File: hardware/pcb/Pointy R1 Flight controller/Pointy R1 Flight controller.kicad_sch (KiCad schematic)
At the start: 28 parts, among them IC1 TEENSY_4.1, J3 XT60-M, M1 Motor_Servo, M2 Motor_Servo, P1 282837-2, P2 282837-2, P3 282837-2, P5 282837-2, Q1 2N7002, Q2 2N7002, Q3 2N7002, U1 L7805CV, U2 GY-521, U3 MPL3115A2

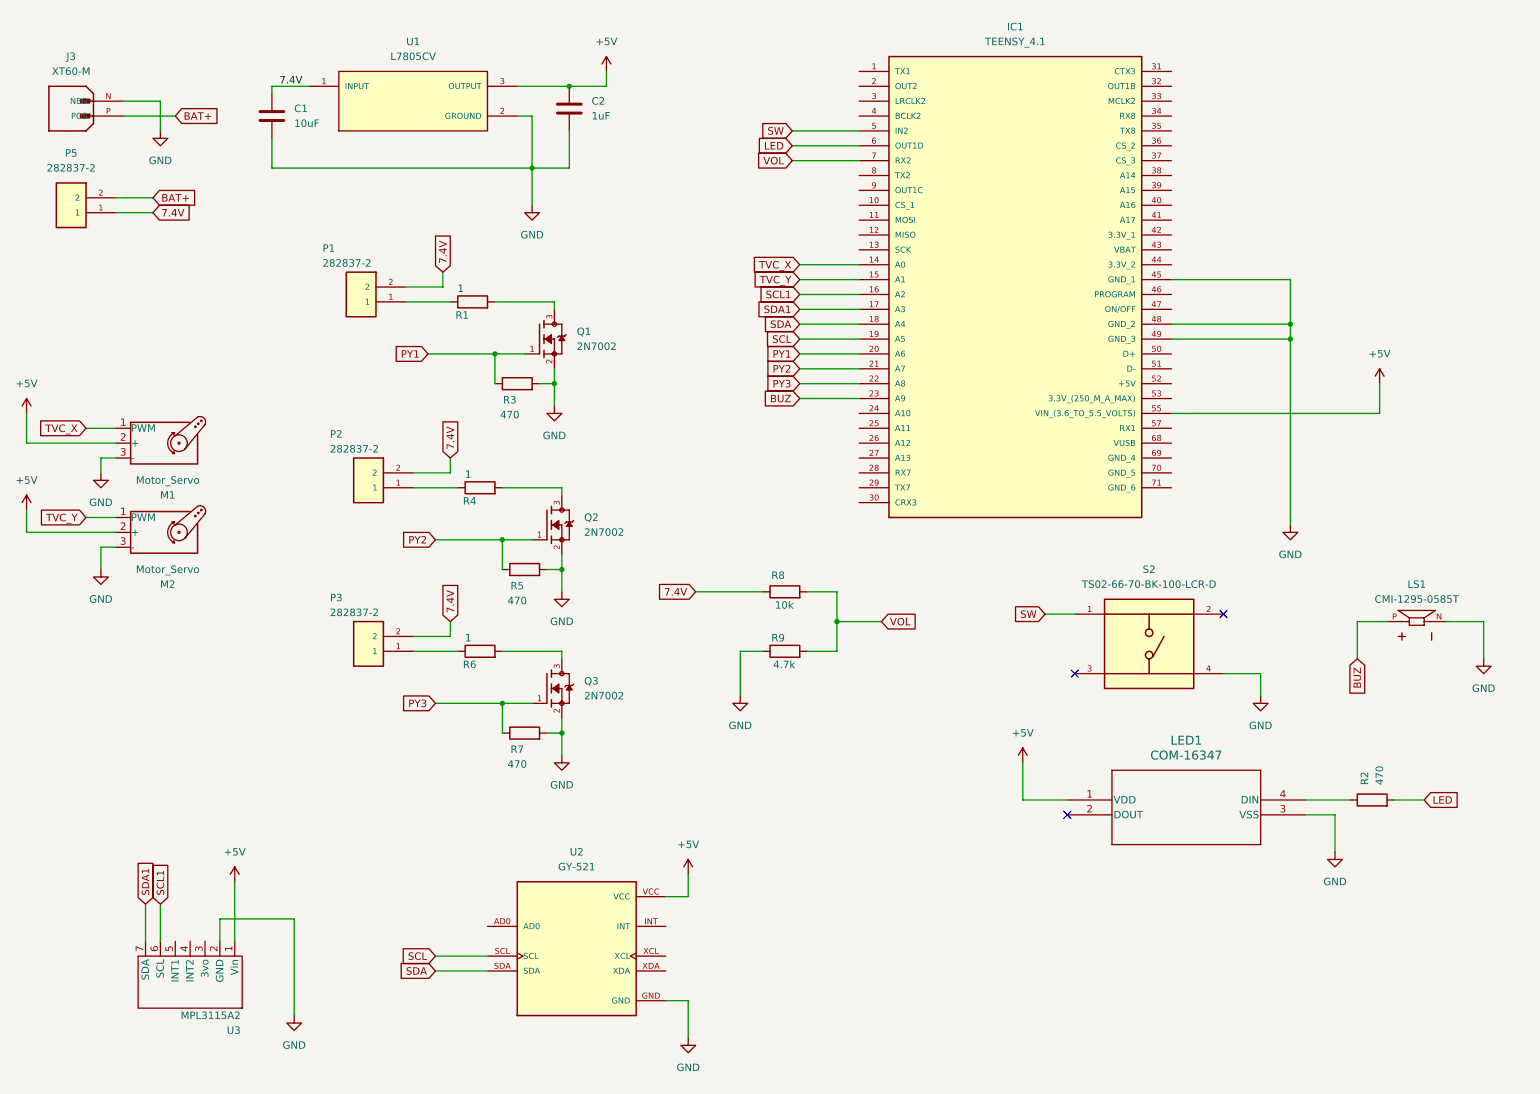
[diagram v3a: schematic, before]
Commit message: added schottky diode for reverse polarity protection, neatened +formated sch
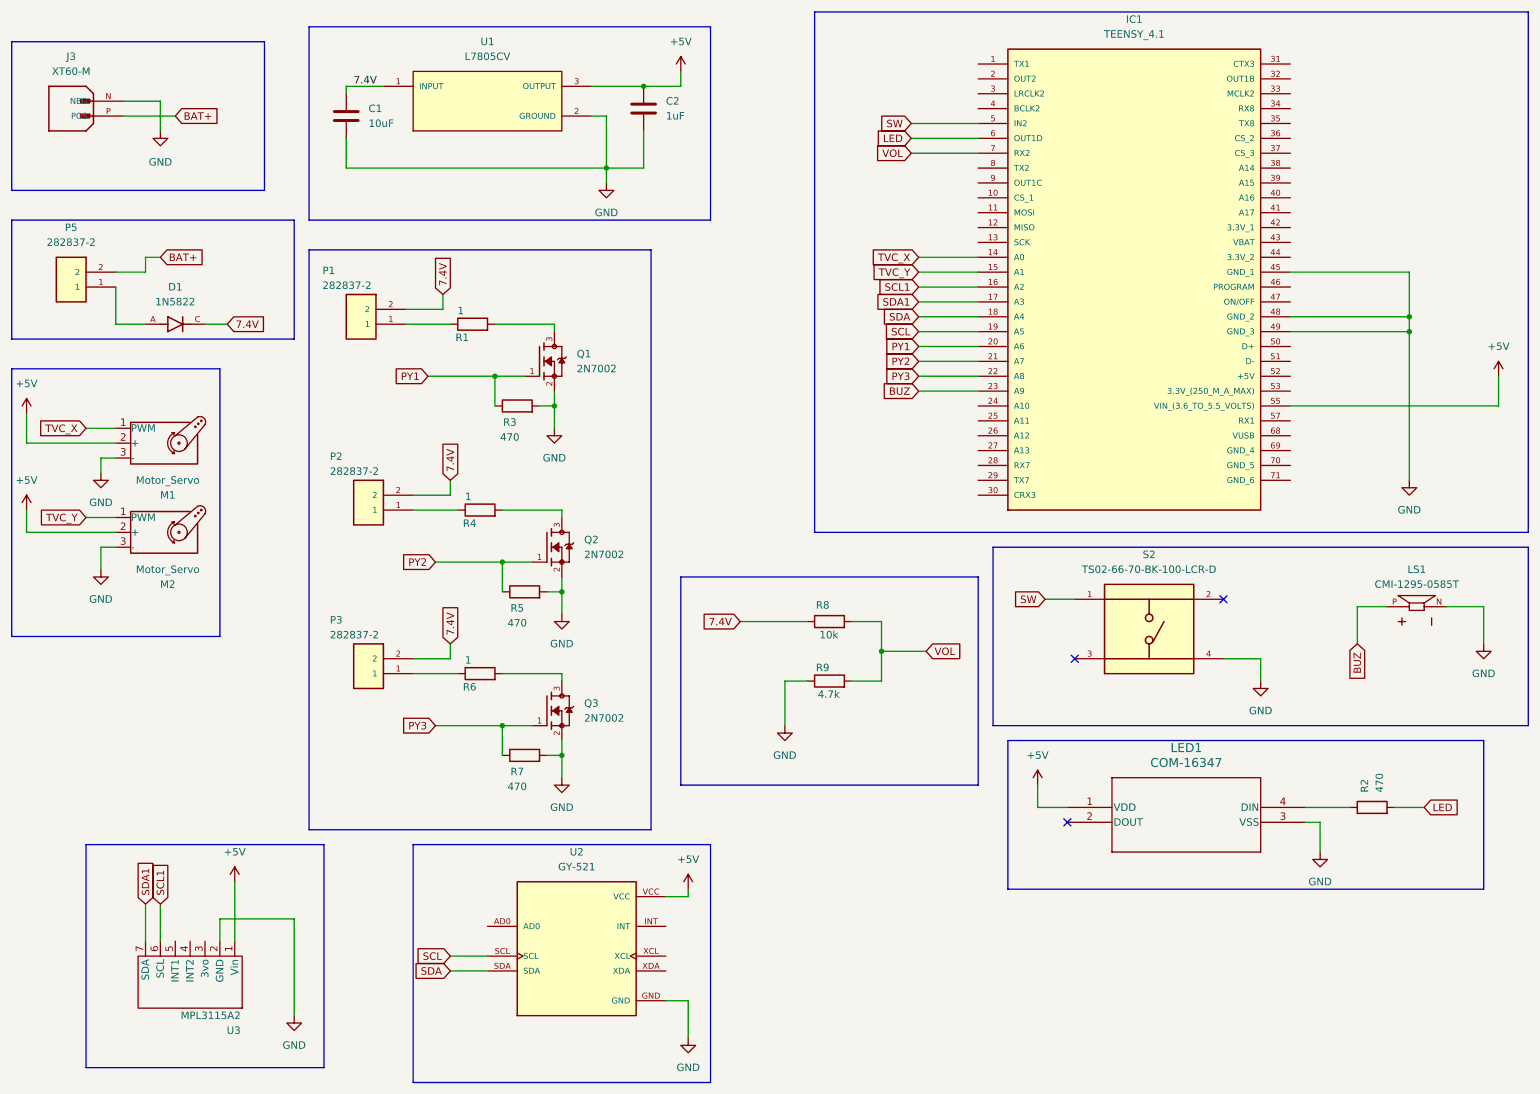
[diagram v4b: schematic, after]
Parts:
- added D1: 1N5822, footprints:DIOAD1990W125L900D530, symbol symbols:1N5822
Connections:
- net 7.4V: now also D1.C; no longer P5.1
- new net: D1.A, P5.1
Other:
- moved on the sheet: C1, C2, IC1, LED1, LS1, P1, P2, P3, P5, Q1, Q2, Q3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

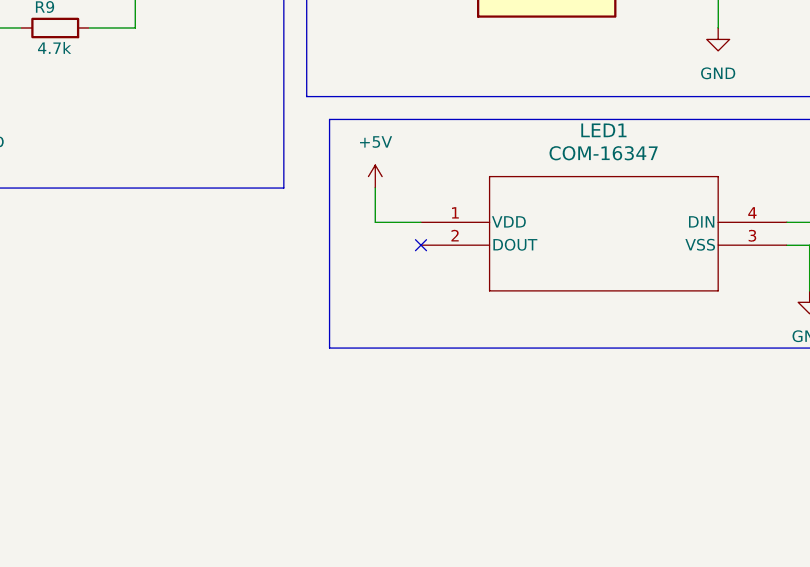
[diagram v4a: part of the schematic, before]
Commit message: Added decoupling cap to WS2812b
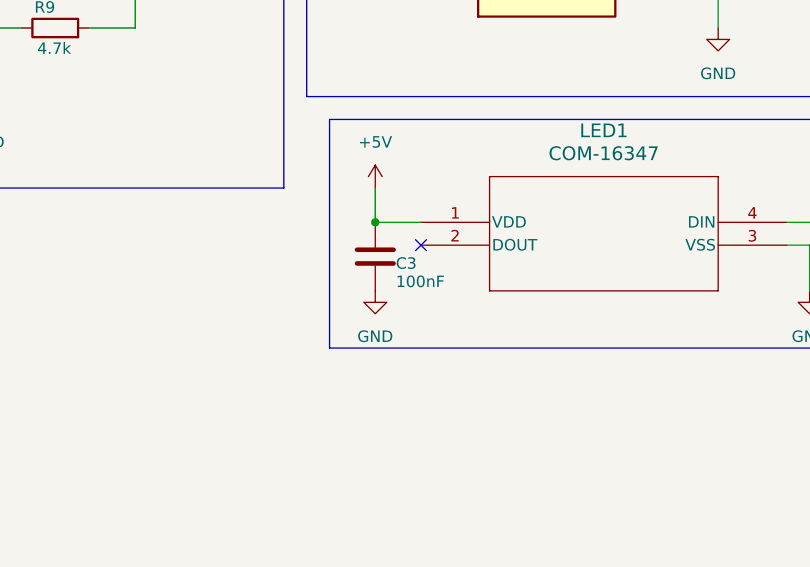
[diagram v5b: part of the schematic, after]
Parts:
- added C3: 100nF, Capacitor_SMD:C_0805_2012Metric, symbol Device:C
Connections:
- net +5V: now also C3.1
- net GND: now also C3.2
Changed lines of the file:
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@@
 	)
 	(junction
+		(at 193.04 148.59)
+		(diameter 0)
+		(color 0 0 0 0)
+	)
+	(junction
 		(at 101.6 106.68)
 		(diameter 0)
@@
 	)
 	(symbol
+		(lib_id "Device:C")
+		(at 193.04 152.4 0)
+		(unit 1)
+		(exclude_from_sim no)
+		(in_bom yes)
+		(on_board yes)
+		(dnp no)
+		(property "Reference" "C3"
+			(at 195.326 153.162 0)
+			(effects
+				(font
+					(size 1.27 1.27)
+				)
+				(justify left)
+			)
+		)
+		(property "Value" "100nF"
+			(at 195.326 155.194 0)
+			(effects
+				(font
+					(size 1.27 1.27)
+				)
+				(justify left)
+			)
+		)
+		(property "Footprint" "Capacitor_SMD:C_0805_2012Metric"
+			(at 194.0052 156.21 0)
+			(effects
+				(font
+					(size 1.27 1.27)
+				)
+				(hide yes)
+			)
+		)
+		(property "Datasheet" "~"
+			(at 193.04 152.4 0)
+			(effects
+				(font
+					(size 1.27 1.27)
+				)
+				(hide yes)
+			)
+		)
+		(property "Description" "Unpolarized capacitor"
+			(at 193.04 152.4 0)
+			(effects
+				(font
+					(size 1.27 1.27)
+				)
+				(hide yes)
+			)
+		)
+		(pin "1"
+		)
+		(pin "2"
+		)
+		(instances
+			(project "Pointy R1 Flight controller"
+				(path "/461b38ed-136a-4336-8029-84a41326c46a"
+					(reference "C3")
+					(unit 1)
+				)
+			)
+		)
+	)
+	(symbol
 		(lib_id "power:GND")
 		(at 133.35 187.96 0)
@@
 					(unit 1)
 				)
+			)
+		)
+	)
+	(symbol
+		(lib_id "power:GND")
+		(at 193.04 156.21 0)
+		(unit 1)
+		(exclude_from_sim no)
+		(in_bom yes)
+		(on_board yes)
+		(dnp no)
+		(fields_autoplaced yes)
+		(property "Reference" "#PWR022"
+			(at 193.04 162.56 0)
+			(effects
+				(font
+					(size 1.27 1.27)
+				)
+				(hide yes)
+			)
+		)
+		(property "Value" "GND"
+			(at 193.04 161.29 0)
+			(effects
+				(font
+					(size 1.27 1.27)
+				)
+			)
+		)
+		(property "Footprint" ""
+			(at 193.04 156.21 0)
+			(effects
+				(font
+					(size 1.27 1.27)
+				)
+				(hide yes)
+			)
+		)
+		(property "Datasheet" ""
+			(at 193.04 156.21 0)
+			(effects
+				(font
+					(size 1.27 1.27)
+				)
+				(hide yes)
+			)
+		)
+		(property "Description" "Power symbol creates a global label with name \"GND\" , ground"
+			(at 193.04 156.21 0)
+			(effects
+				(font
+					(size 1.27 1.27)
+				)
+				(hide yes)
+			)
+		)
+		(pin "1"
+		)
+		(instances
+			(project ""
+				(path "/461b38ed-136a-4336-8029-84a41326c46a"
+					(reference "#PWR022")
+					(unit 1)
+				)

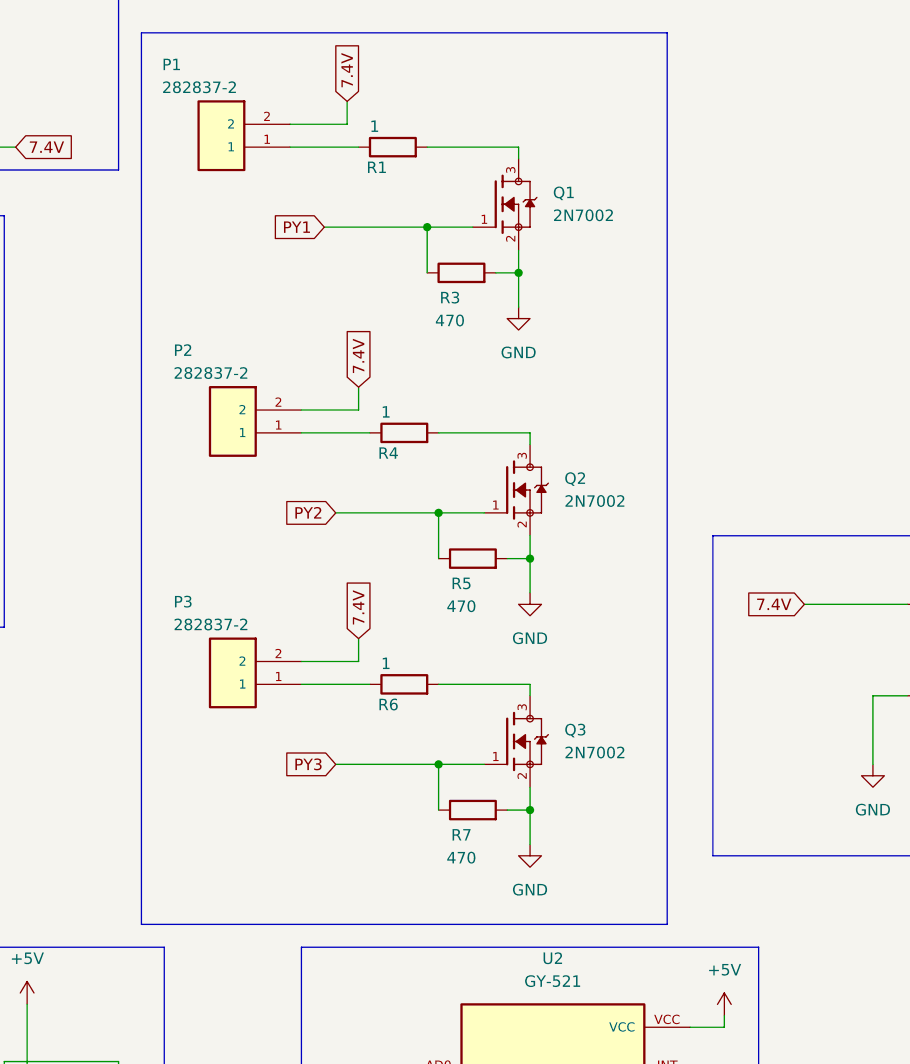
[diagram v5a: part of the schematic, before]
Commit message: Replaced mosfets with higher current rated IRLZ44N
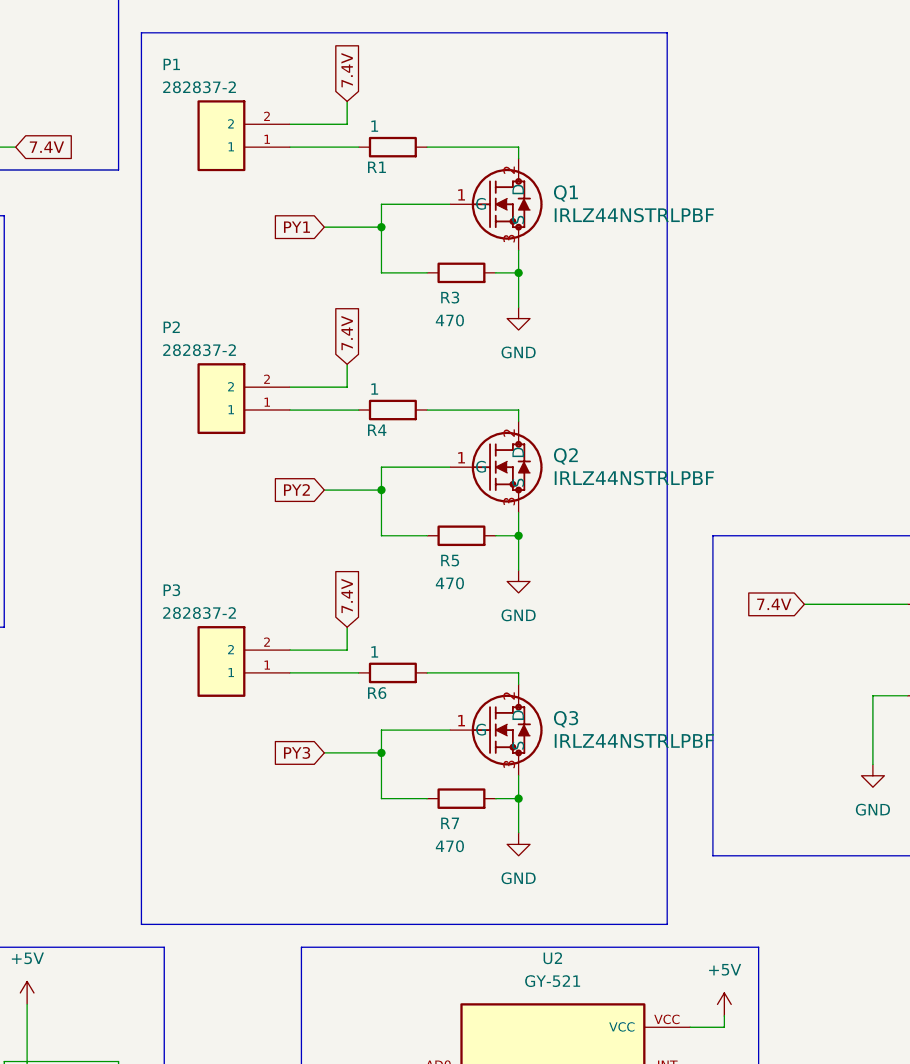
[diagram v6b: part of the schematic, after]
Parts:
- removed Q1, Q2, Q3: 2N7002, footprints:SOT95P240X111-3N, symbol symbols:2N7002
- added Q1, Q2, Q3: IRLZ44NSTRLPBF, footprints:NMOSGDS_D2PAK_INF, symbol symbols:IRLZ44NSTRLPBF
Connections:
- net GND: now also Q1.3 (S), Q2.3 (S), Q3.3 (S)
- net PY1: now also Q1.1 (G)
- net PY2: now also Q2.1 (G)
- net PY3: now also Q3.1 (G)
- net at R6.2: now also Q3.2 (D)
- net at R1.2: now also Q1.2 (D)
- net at R4.2: now also Q2.2 (D)
